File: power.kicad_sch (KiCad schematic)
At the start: 26 parts, among them U3 EA3036, U8 TLV71312PDBV

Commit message: update mini
Signed-off-by: huangzzk <huangcmzzk@gmail.com>
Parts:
- added C57, C58: 10u, Capacitor_SMD:C_0603_1608Metric, symbol Device:C
- added C59: 1u, Capacitor_SMD:C_0402_1005Metric, symbol Device:C
- added C60: 0.1u, Capacitor_SMD:C_0402_1005Metric, symbol Device:C
- added D4: LED, LED_SMD:LED_0603_1608Metric, symbol Device:LED
- added J2, J5, J6, J7: Conn_01x03, Connector_Molex:Molex_CLIK-Mate_502386-0370_1x03-1MP_P1.25mm_Horizontal, symbol Connector_Generic:Conn_01x03
- added J3: Conn_01x02, Connector_PinHeader_2.54mm:PinHeader_1x02_P2.54mm_Vertical, symbol Connector_Generic:Conn_01x02
- added L1: L, Inductor_SMD:L_Abracon_ASPI-3012S, symbol Device:L
- added Q1, Q2: Q_NMOS_GSD, Package_TO_SOT_SMD:SOT-23, symbol Device:Q_NMOS_GSD
- added R17: 0R, Resistor_SMD:R_0402_1005Metric, symbol Device:R
- added R27, R28, R29: 10K, Resistor_SMD:R_0402_1005Metric, symbol Device:R
- added U9: ETA9640, Package_SO:SOIC-8-1EP_3.9x4.9mm_P1.27mm_EP2.41x3.3mm, symbol SCH_IntegratedCircuit:ETA9640
- C31, C34: value 4.7uF -> 4.7u
- R20: value 0R -> 1.2k
- U8: value TLV71312PDBV -> ME6212C12M5G
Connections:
- net +5V: now also C59.1, C60.1, U9.5 (OUT); no longer R20.1
- net GND: now also R20.2, C58.1, C59.2, C60.2, D4.1 (K), R17.1, U9.6 (GND)
- net VBUS: now also C58.2, U9.1 (VIN); no longer R20.2
- new net: L1.2, U9.4 (SW)
- new net: J5.3 (Pin_3), Q2.3 (D)
- new net: R20.1, U9.8 (ISET)
- new net: J2.3 (Pin_3), Q1.3 (D)
- new net: D4.2 (A), R27.1
- new net: R27.2, U9.7 (LED)
- new net +BATT: C57.1, J2.2 (Pin_2), J3.1 (Pin_1), J5.2 (Pin_2), J6.2 (Pin_2), J7.2 (Pin_2), L1.1, U9.2 (BAT), U9.3 (EN)
- new net GNDPWR: C57.2, J3.2 (Pin_2), J6.3 (Pin_3), J7.3 (Pin_3), Q1.2 (S), Q2.2 (S), R17.2, R28.2, R29.2, U9.9 (BGND)
- new net PWM1: J2.1 (Pin_1), Q1.1 (G), R28.1
- new net PWM2: J5.1 (Pin_1), Q2.1 (G), R29.1
- new net PWM3: J6.1 (Pin_1)
- new net PWM4: J7.1 (Pin_1)
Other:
- note removed: "replaced by ME6212C12M5G"

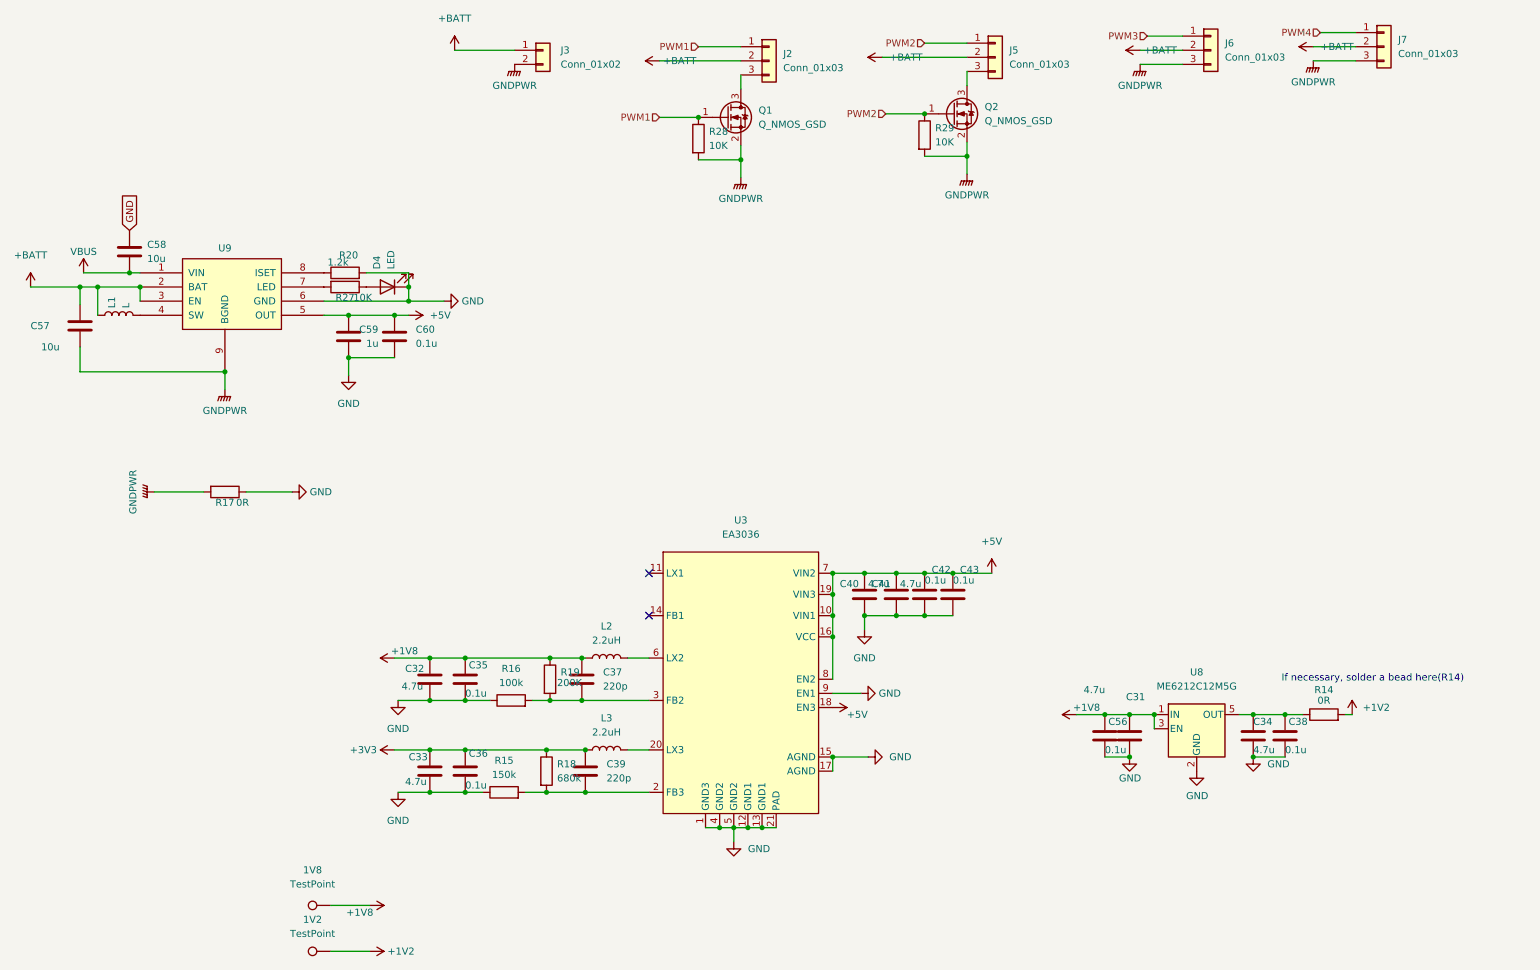
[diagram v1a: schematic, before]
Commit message: add esp32 as wifi card
Signed-off-by: huangzzk <huangcmzzk@gmail.com>
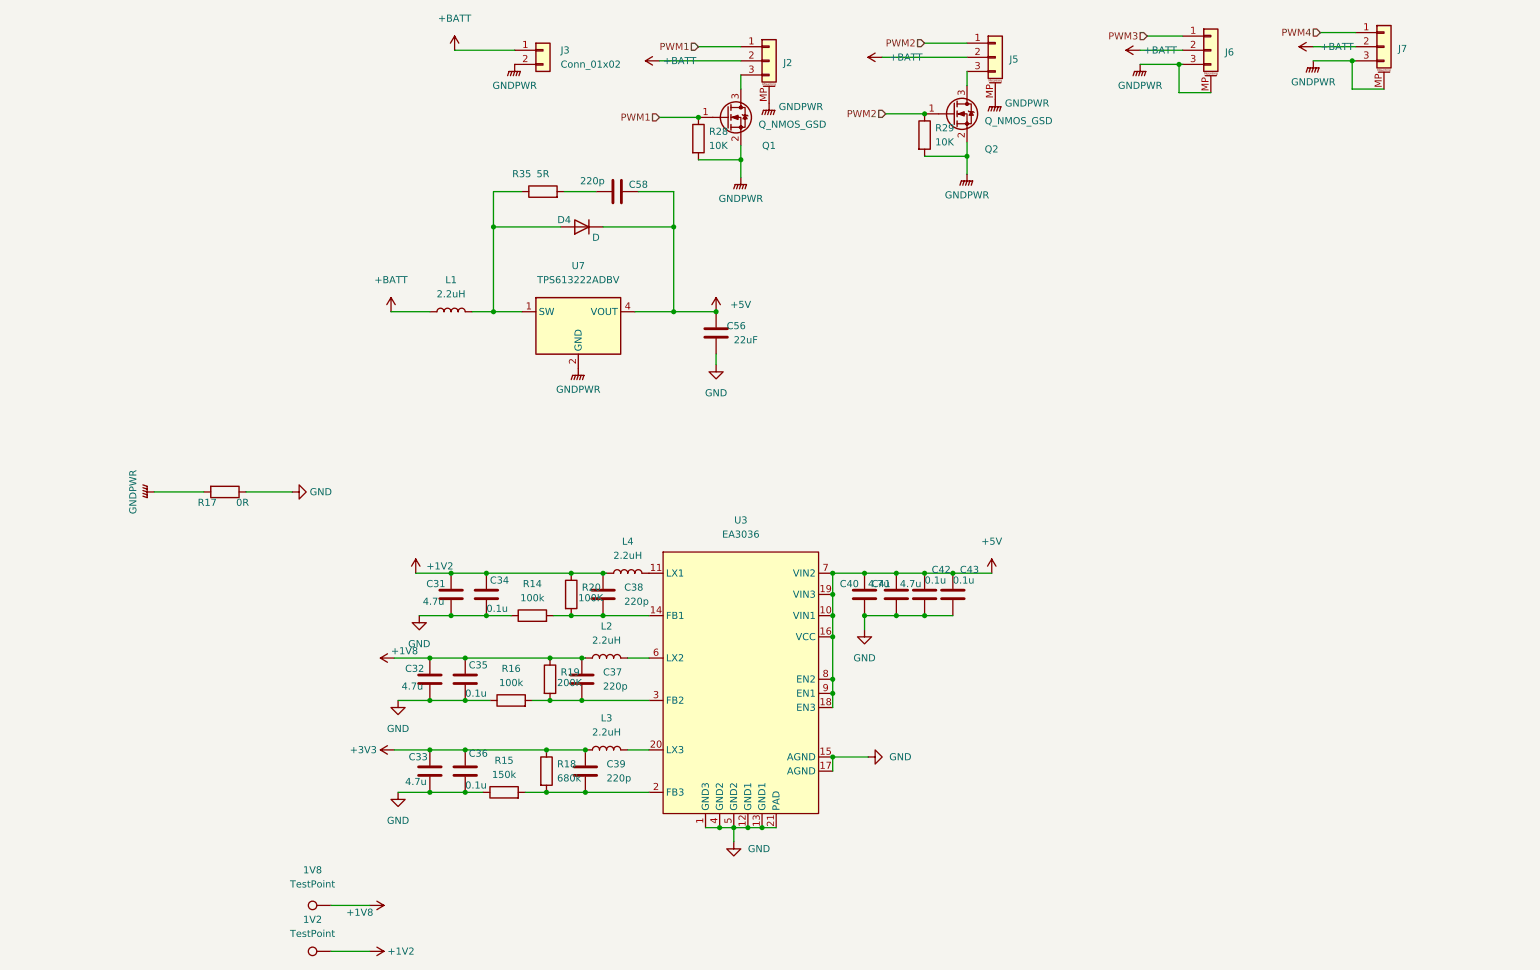
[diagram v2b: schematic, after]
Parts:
- removed C57: 10u, Capacitor_SMD:C_0603_1608Metric, symbol Device:C
- removed C59: 1u, Capacitor_SMD:C_0402_1005Metric, symbol Device:C
- removed C60: 0.1u, Capacitor_SMD:C_0402_1005Metric, symbol Device:C
- removed D4: LED, LED_SMD:LED_0603_1608Metric, symbol Device:LED
- removed J2, J5, J6, J7: Conn_01x03, Connector_Molex:Molex_CLIK-Mate_502386-0370_1x03-1MP_P1.25mm_Horizontal, symbol Connector_Generic:Conn_01x03
- removed R27: 10K, Resistor_SMD:R_0402_1005Metric, symbol Device:R
- removed U8: ME6212C12M5G, Package_TO_SOT_SMD:SOT-23-5, symbol Regulator_Linear:TLV71312PDBV
- removed U9: ETA9640, Package_SO:SOIC-8-1EP_3.9x4.9mm_P1.27mm_EP2.41x3.3mm, symbol SCH_IntegratedCircuit:ETA9640
- added D4: D, Diode_SMD:D_0805_2012Metric, symbol Device:D
- added J2, J5, J6, J7: Conn_01x03_MountingPin, Connector_Molex:Molex_CLIK-Mate_502386-0370_1x03-1MP_P1.25mm_Horizontal, symbol Connector_Generic_MountingPin:Conn_01x03_MountingPin
- added L4: 2.2uH, Inductor_SMD:L_Abracon_ASPI-3012S, symbol Device:L
- added R35: 5R, Resistor_SMD:R_0402_1005Metric, symbol Device:R
- added U7: TPS613222ADBV, Package_TO_SOT_SMD:SOT-23-5, symbol Regulator_Switching:TPS613222ADBV
- C34: value 4.7u -> 0.1u
- C38: value 0.1u -> 220p
- C56: value 0.1u -> 22uF; footprint Capacitor_SMD:C_0402_1005Metric -> Capacitor_SMD:C_0603_1608Metric
- C58: value 10u -> 220p; footprint Capacitor_SMD:C_0603_1608Metric -> Capacitor_SMD:C_0402_1005Metric
- L1: value L -> 2.2uH
- R14: value 0R -> 100k
- R20: value 1.2k -> 100K
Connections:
- net VBUS is gone; now on net +5V: C58.2
- net +1V2: now also C31.1, C34.1, C38.1, R20.1, L4.1; no longer R14.2
- net +1V8: no longer C31.1, C56.1
- net +5V: now also C56.1, U3.9 (EN1), D4.1 (K), U7.4 (VOUT)
- net +BATT: now also J2.2 (Pin_2), J5.2 (Pin_2), J6.2 (Pin_2), J7.2 (Pin_2)
- net GND: now also R14.1; no longer C38.2, C58.1, R20.2, U3.9 (EN1)
- net GNDPWR: now also J2.MP (MountPin), J5.MP (MountPin), J6.3 (Pin_3), J6.MP (MountPin), J7.3 (Pin_3), J7.MP (MountPin), U7.2 (GND)
- net PWM1: now also J2.1 (Pin_1)
- net PWM2: now also J5.1 (Pin_1)
- net PWM3: now also J6.1 (Pin_1)
- net PWM4: now also J7.1 (Pin_1)
- net at L1.2: now also D4.2 (A), R35.1, U7.1 (SW)
- net at Q2.3 (D): now also J5.3 (Pin_3)
- net at Q1.3 (D): now also J2.3 (Pin_3)
- net at U3.11 (LX1): now also L4.2
- net at U3.14 (FB1): now also C38.2, R14.2, R20.2
- new net: C58.1, R35.2
- no-connect marks 2 -> 0
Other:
- note removed: "If necessary, solder a bead here(R14)"
